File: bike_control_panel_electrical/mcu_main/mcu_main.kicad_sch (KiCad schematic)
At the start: 11 parts, among them U1 ESP32-S3-WROOM-1, U2 USB_C_connector

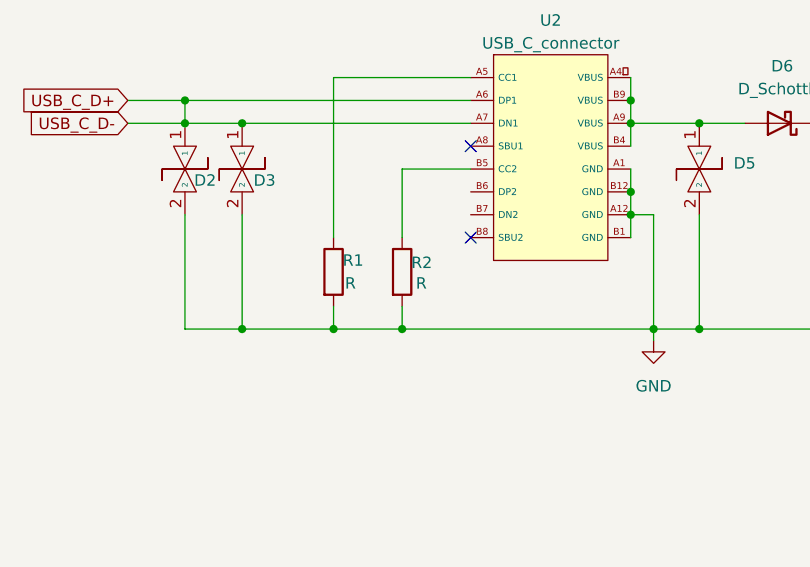
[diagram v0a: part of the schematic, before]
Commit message: changed resistor value for the cc pins on the type c connector
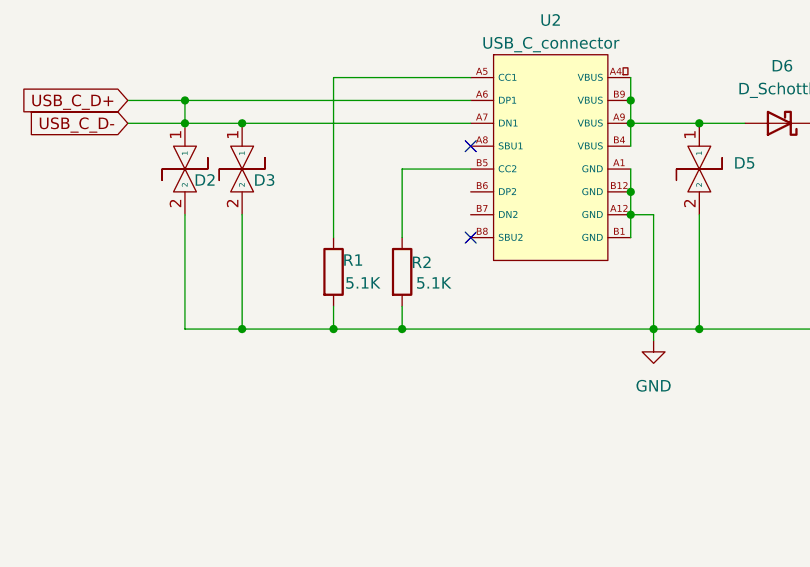
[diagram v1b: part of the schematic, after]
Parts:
- R1, R2: value R -> 5.1K
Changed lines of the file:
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@@
 			)
 		)
-		(property "Value" "R"
+		(property "Value" "5.1K"
 			(at 165.354 53.34 0)
 			(effects
@@
 			)
 		)
-		(property "Value" "R"
+		(property "Value" "5.1K"
 			(at 157.48 53.34 0)
 			(effects
